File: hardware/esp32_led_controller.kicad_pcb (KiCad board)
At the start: 4 copper layers, 61 x 42.5 mm, 28 parts, among them J1 USB_B, J2 BARREL_JACK, J3 Screw_Terminal_1x03, J4 CONN_01X11, J5 CONN_01X09, Q1 Q_NPN_BEC, Q4 Q_NPN_BEC, SW1 SW_Push, U1 MCP1415, U11 AZ1117-3.3, U3 CP2102, U4 ESP32-WROOM-32

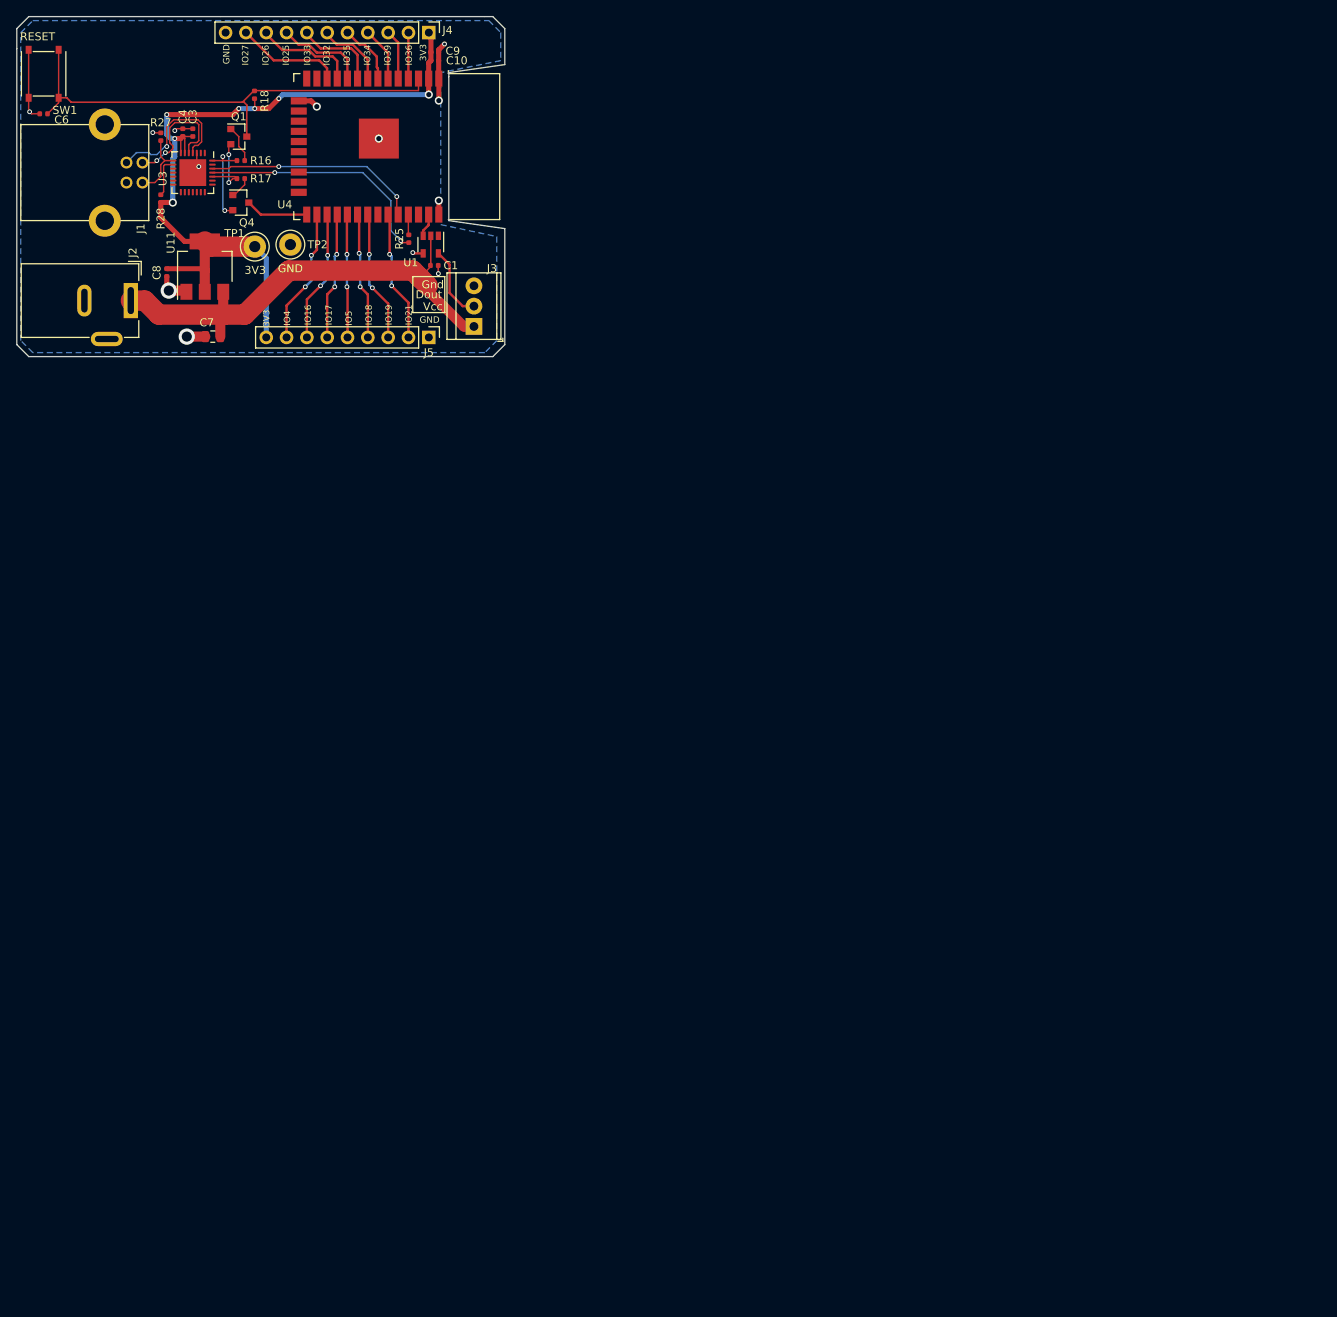
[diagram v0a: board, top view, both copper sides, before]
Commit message: Finished design with integrated LED matrix
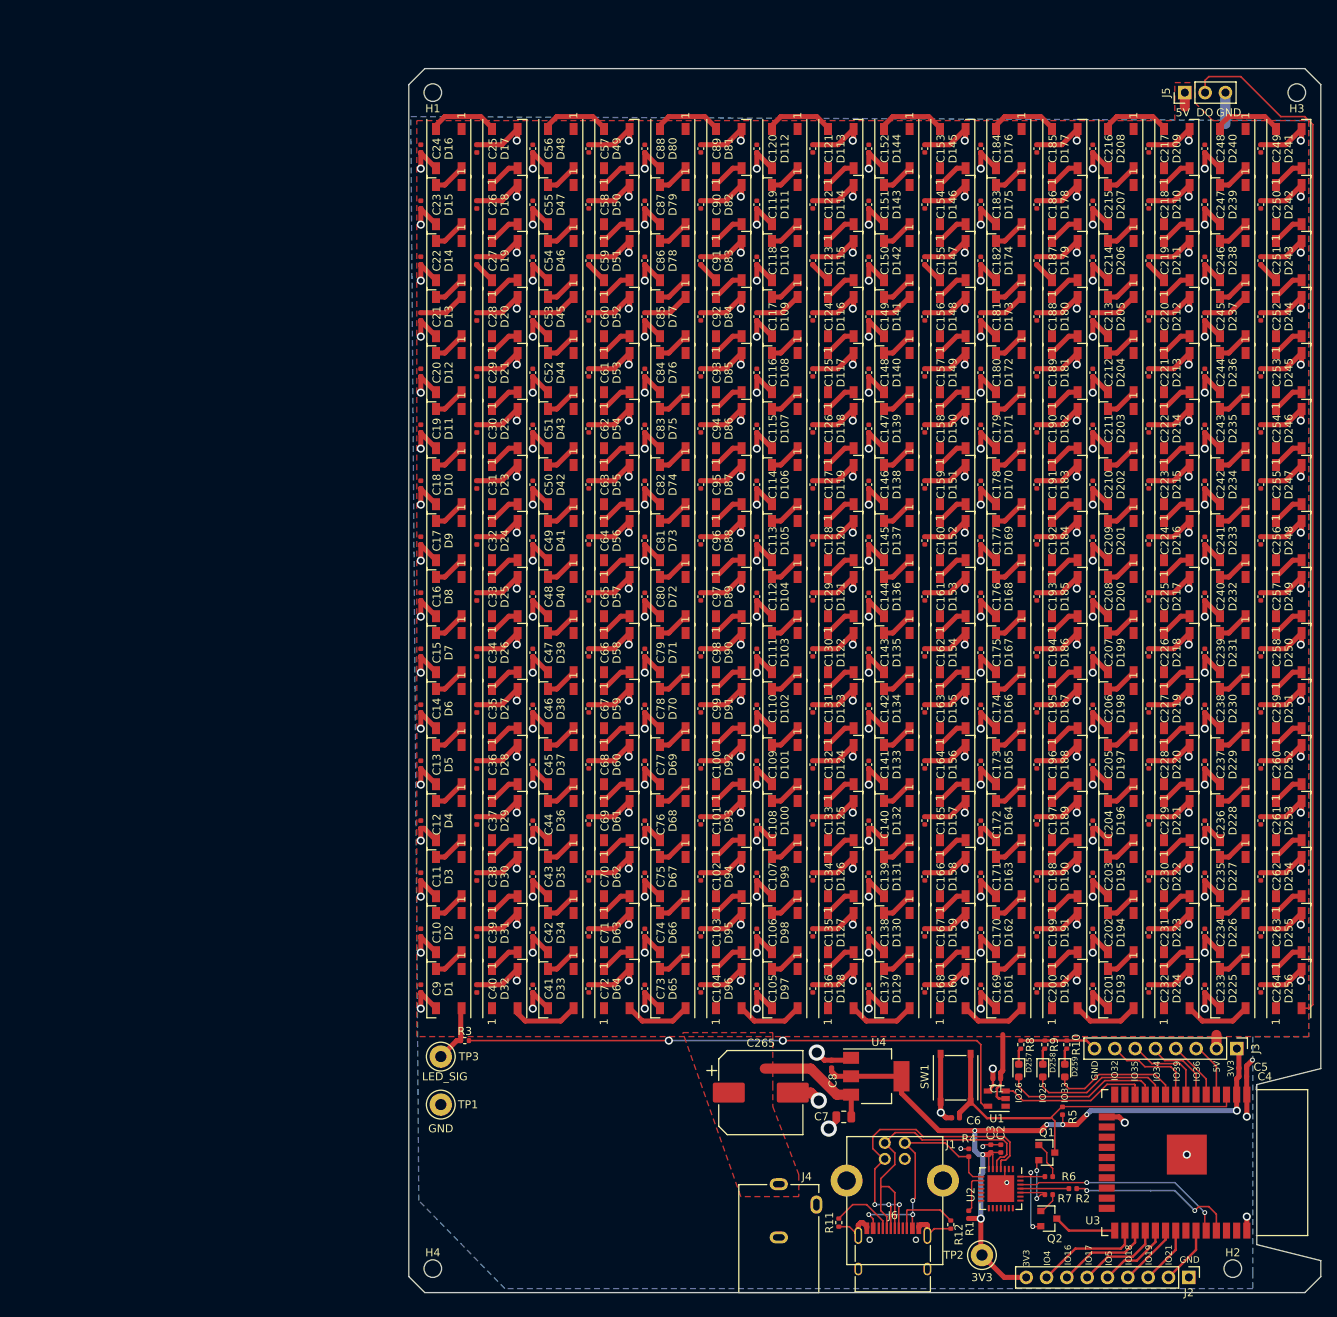
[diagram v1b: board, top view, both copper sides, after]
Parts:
- removed the J2 at (93.2, 75.0)
- added C10: 0.1uF, Capacitor_SMD:C_0402_1005Metric, F.Cu at (129.5, 154.0)
- added C100: 0.1uF, Capacitor_SMD:C_0402_1005Metric, F.Cu at (164.5, 133.0)
- added C101: 0.1uF, Capacitor_SMD:C_0402_1005Metric, F.Cu at (164.5, 140.0)
- added C102: 0.1uF, Capacitor_SMD:C_0402_1005Metric, F.Cu at (164.5, 147.0)
- added C103: 0.1uF, Capacitor_SMD:C_0402_1005Metric, F.Cu at (164.5, 154.0)
- added C104: 0.1uF, Capacitor_SMD:C_0402_1005Metric, F.Cu at (164.5, 161.0)
- added C105: 0.1uF, Capacitor_SMD:C_0402_1005Metric, F.Cu at (171.5, 161.0)
- added C106: 0.1uF, Capacitor_SMD:C_0402_1005Metric, F.Cu at (171.5, 154.0)
- added C107: 0.1uF, Capacitor_SMD:C_0402_1005Metric, F.Cu at (171.5, 147.0)
- added C108: 0.1uF, Capacitor_SMD:C_0402_1005Metric, F.Cu at (171.5, 140.5)
- added C109: 0.1uF, Capacitor_SMD:C_0402_1005Metric, F.Cu at (171.5, 133.0)
- added C11: 0.1uF, Capacitor_SMD:C_0402_1005Metric, F.Cu at (129.5, 147.0)
- added C110: 0.1uF, Capacitor_SMD:C_0402_1005Metric, F.Cu at (171.5, 126.0)
- added C111: 0.1uF, Capacitor_SMD:C_0402_1005Metric, F.Cu at (171.5, 119.0)
- added C112: 0.1uF, Capacitor_SMD:C_0402_1005Metric, F.Cu at (171.5, 112.0)
- added C113: 0.1uF, Capacitor_SMD:C_0402_1005Metric, F.Cu at (171.5, 105.0)
- added C114: 0.1uF, Capacitor_SMD:C_0402_1005Metric, F.Cu at (171.5, 98.0)
- added C115: 0.1uF, Capacitor_SMD:C_0402_1005Metric, F.Cu at (171.5, 91.0)
- added C116: 0.1uF, Capacitor_SMD:C_0402_1005Metric, F.Cu at (171.5, 84.0)
- added C117: 0.1uF, Capacitor_SMD:C_0402_1005Metric, F.Cu at (171.5, 77.0)
- added C118: 0.1uF, Capacitor_SMD:C_0402_1005Metric, F.Cu at (171.5, 70.0)
- added C119: 0.1uF, Capacitor_SMD:C_0402_1005Metric, F.Cu at (171.5, 63.0)
- added C12: 0.1uF, Capacitor_SMD:C_0402_1005Metric, F.Cu at (129.5, 140.5)
- added C120: 0.1uF, Capacitor_SMD:C_0402_1005Metric, F.Cu at (171.5, 56.0)
- added C121: 0.1uF, Capacitor_SMD:C_0402_1005Metric, F.Cu at (178.5, 56.0)
- added C122: 0.1uF, Capacitor_SMD:C_0402_1005Metric, F.Cu at (178.5, 63.0)
- added C123: 0.1uF, Capacitor_SMD:C_0402_1005Metric, F.Cu at (178.5, 70.0)
- added C124: 0.1uF, Capacitor_SMD:C_0402_1005Metric, F.Cu at (178.5, 77.0)
- added C125: 0.1uF, Capacitor_SMD:C_0402_1005Metric, F.Cu at (178.5, 84.0)
- added C126: 0.1uF, Capacitor_SMD:C_0402_1005Metric, F.Cu at (178.5, 91.0)
- added C127: 0.1uF, Capacitor_SMD:C_0402_1005Metric, F.Cu at (178.5, 98.0)
- added C128: 0.1uF, Capacitor_SMD:C_0402_1005Metric, F.Cu at (178.5, 105.0)
- added C129: 0.1uF, Capacitor_SMD:C_0402_1005Metric, F.Cu at (178.5, 112.0)
- added C13: 0.1uF, Capacitor_SMD:C_0402_1005Metric, F.Cu at (129.5, 133.0)
- added C130: 0.1uF, Capacitor_SMD:C_0402_1005Metric, F.Cu at (178.5, 119.0)
- added C131: 0.1uF, Capacitor_SMD:C_0402_1005Metric, F.Cu at (178.5, 126.0)
- added C132: 0.1uF, Capacitor_SMD:C_0402_1005Metric, F.Cu at (178.5, 133.0)
- added C133: 0.1uF, Capacitor_SMD:C_0402_1005Metric, F.Cu at (178.5, 140.0)
- added C134: 0.1uF, Capacitor_SMD:C_0402_1005Metric, F.Cu at (178.5, 147.0)
- added C135: 0.1uF, Capacitor_SMD:C_0402_1005Metric, F.Cu at (178.5, 154.0)
- added C136: 0.1uF, Capacitor_SMD:C_0402_1005Metric, F.Cu at (178.5, 161.0)
- added C137: 0.1uF, Capacitor_SMD:C_0402_1005Metric, F.Cu at (185.5, 161.0)
- added C138: 0.1uF, Capacitor_SMD:C_0402_1005Metric, F.Cu at (185.5, 154.0)
- added C139: 0.1uF, Capacitor_SMD:C_0402_1005Metric, F.Cu at (185.5, 147.0)
- added C14: 0.1uF, Capacitor_SMD:C_0402_1005Metric, F.Cu at (129.5, 126.0)
- added C140: 0.1uF, Capacitor_SMD:C_0402_1005Metric, F.Cu at (185.5, 140.5)
- added C141: 0.1uF, Capacitor_SMD:C_0402_1005Metric, F.Cu at (185.5, 133.0)
- added C142: 0.1uF, Capacitor_SMD:C_0402_1005Metric, F.Cu at (185.5, 126.0)
- added C143: 0.1uF, Capacitor_SMD:C_0402_1005Metric, F.Cu at (185.5, 119.0)
- added C144: 0.1uF, Capacitor_SMD:C_0402_1005Metric, F.Cu at (185.5, 112.0)
- added C145: 0.1uF, Capacitor_SMD:C_0402_1005Metric, F.Cu at (185.5, 105.0)
- added C146: 0.1uF, Capacitor_SMD:C_0402_1005Metric, F.Cu at (185.5, 98.0)
- added C147: 0.1uF, Capacitor_SMD:C_0402_1005Metric, F.Cu at (185.5, 91.0)
- added C148: 0.1uF, Capacitor_SMD:C_0402_1005Metric, F.Cu at (185.5, 84.0)
- added C149: 0.1uF, Capacitor_SMD:C_0402_1005Metric, F.Cu at (185.5, 77.0)
- added C15: 0.1uF, Capacitor_SMD:C_0402_1005Metric, F.Cu at (129.5, 119.0)
- added C150: 0.1uF, Capacitor_SMD:C_0402_1005Metric, F.Cu at (185.5, 70.0)
- added C151: 0.1uF, Capacitor_SMD:C_0402_1005Metric, F.Cu at (185.5, 63.0)
- added C152: 0.1uF, Capacitor_SMD:C_0402_1005Metric, F.Cu at (185.5, 56.0)
- added C153: 0.1uF, Capacitor_SMD:C_0402_1005Metric, F.Cu at (192.5, 56.0)
- added C154: 0.1uF, Capacitor_SMD:C_0402_1005Metric, F.Cu at (192.5, 63.0)
- added C155: 0.1uF, Capacitor_SMD:C_0402_1005Metric, F.Cu at (192.5, 70.0)
- added C156: 0.1uF, Capacitor_SMD:C_0402_1005Metric, F.Cu at (192.5, 77.0)
- added C157: 0.1uF, Capacitor_SMD:C_0402_1005Metric, F.Cu at (192.5, 84.0)
- added C158: 0.1uF, Capacitor_SMD:C_0402_1005Metric, F.Cu at (192.5, 91.0)
- added C159: 0.1uF, Capacitor_SMD:C_0402_1005Metric, F.Cu at (192.5, 98.0)
- added C16: 0.1uF, Capacitor_SMD:C_0402_1005Metric, F.Cu at (129.5, 112.0)
- added C160: 0.1uF, Capacitor_SMD:C_0402_1005Metric, F.Cu at (192.5, 105.0)
- added C161: 0.1uF, Capacitor_SMD:C_0402_1005Metric, F.Cu at (192.5, 112.0)
- added C162: 0.1uF, Capacitor_SMD:C_0402_1005Metric, F.Cu at (192.5, 119.0)
- added C163: 0.1uF, Capacitor_SMD:C_0402_1005Metric, F.Cu at (192.5, 126.0)
- added C164: 0.1uF, Capacitor_SMD:C_0402_1005Metric, F.Cu at (192.5, 133.0)
- added C165: 0.1uF, Capacitor_SMD:C_0402_1005Metric, F.Cu at (192.5, 140.0)
- added C166: 0.1uF, Capacitor_SMD:C_0402_1005Metric, F.Cu at (192.5, 147.0)
- added C167: 0.1uF, Capacitor_SMD:C_0402_1005Metric, F.Cu at (192.5, 154.0)
- added C168: 0.1uF, Capacitor_SMD:C_0402_1005Metric, F.Cu at (192.5, 161.0)
- added C169: 0.1uF, Capacitor_SMD:C_0402_1005Metric, F.Cu at (199.5, 161.0)
- added C17: 0.1uF, Capacitor_SMD:C_0402_1005Metric, F.Cu at (129.5, 105.0)
- added C170: 0.1uF, Capacitor_SMD:C_0402_1005Metric, F.Cu at (199.5, 154.0)
- added C171: 0.1uF, Capacitor_SMD:C_0402_1005Metric, F.Cu at (199.5, 147.0)
- added C172: 0.1uF, Capacitor_SMD:C_0402_1005Metric, F.Cu at (199.5, 140.5)
- added C173: 0.1uF, Capacitor_SMD:C_0402_1005Metric, F.Cu at (199.5, 133.0)
- added C174: 0.1uF, Capacitor_SMD:C_0402_1005Metric, F.Cu at (199.5, 126.0)
- added C175: 0.1uF, Capacitor_SMD:C_0402_1005Metric, F.Cu at (199.5, 119.0)
- added C176: 0.1uF, Capacitor_SMD:C_0402_1005Metric, F.Cu at (199.5, 112.0)
- added C177: 0.1uF, Capacitor_SMD:C_0402_1005Metric, F.Cu at (199.5, 105.0)
- added C178: 0.1uF, Capacitor_SMD:C_0402_1005Metric, F.Cu at (199.5, 98.0)
- added C179: 0.1uF, Capacitor_SMD:C_0402_1005Metric, F.Cu at (199.5, 91.0)
- added C18: 0.1uF, Capacitor_SMD:C_0402_1005Metric, F.Cu at (129.5, 98.0)
- added C180: 0.1uF, Capacitor_SMD:C_0402_1005Metric, F.Cu at (199.5, 84.0)
- added C181: 0.1uF, Capacitor_SMD:C_0402_1005Metric, F.Cu at (199.5, 77.0)
- added C182: 0.1uF, Capacitor_SMD:C_0402_1005Metric, F.Cu at (199.5, 70.0)
- added C183: 0.1uF, Capacitor_SMD:C_0402_1005Metric, F.Cu at (199.5, 63.0)
- added C184: 0.1uF, Capacitor_SMD:C_0402_1005Metric, F.Cu at (199.5, 56.0)
- added C185: 0.1uF, Capacitor_SMD:C_0402_1005Metric, F.Cu at (206.5, 56.0)
- added C186: 0.1uF, Capacitor_SMD:C_0402_1005Metric, F.Cu at (206.5, 63.0)
- added C187: 0.1uF, Capacitor_SMD:C_0402_1005Metric, F.Cu at (206.5, 70.0)
- added C188: 0.1uF, Capacitor_SMD:C_0402_1005Metric, F.Cu at (206.5, 77.0)
- added C189: 0.1uF, Capacitor_SMD:C_0402_1005Metric, F.Cu at (206.5, 84.0)
- added C19: 0.1uF, Capacitor_SMD:C_0402_1005Metric, F.Cu at (129.5, 91.0)
- added C190: 0.1uF, Capacitor_SMD:C_0402_1005Metric, F.Cu at (206.5, 91.0)
- added C191: 0.1uF, Capacitor_SMD:C_0402_1005Metric, F.Cu at (206.5, 98.0)
- added C192: 0.1uF, Capacitor_SMD:C_0402_1005Metric, F.Cu at (206.5, 105.0)
- added C193: 0.1uF, Capacitor_SMD:C_0402_1005Metric, F.Cu at (206.5, 112.0)
- added C194: 0.1uF, Capacitor_SMD:C_0402_1005Metric, F.Cu at (206.5, 119.0)
- added C195: 0.1uF, Capacitor_SMD:C_0402_1005Metric, F.Cu at (206.5, 126.0)
- added C196: 0.1uF, Capacitor_SMD:C_0402_1005Metric, F.Cu at (206.5, 133.0)
- added C197: 0.1uF, Capacitor_SMD:C_0402_1005Metric, F.Cu at (206.5, 140.0)
- added C198: 0.1uF, Capacitor_SMD:C_0402_1005Metric, F.Cu at (206.5, 147.0)
- added C199: 0.1uF, Capacitor_SMD:C_0402_1005Metric, F.Cu at (206.5, 154.0)
- added C20: 0.1uF, Capacitor_SMD:C_0402_1005Metric, F.Cu at (129.5, 84.0)
- added C200: 0.1uF, Capacitor_SMD:C_0402_1005Metric, F.Cu at (206.5, 161.0)
- added C201: 0.1uF, Capacitor_SMD:C_0402_1005Metric, F.Cu at (213.5, 161.0)
- added C202: 0.1uF, Capacitor_SMD:C_0402_1005Metric, F.Cu at (213.5, 154.0)
- added C203: 0.1uF, Capacitor_SMD:C_0402_1005Metric, F.Cu at (213.5, 147.0)
- added C204: 0.1uF, Capacitor_SMD:C_0402_1005Metric, F.Cu at (213.5, 140.5)
- added C205: 0.1uF, Capacitor_SMD:C_0402_1005Metric, F.Cu at (213.5, 133.0)
- added C206: 0.1uF, Capacitor_SMD:C_0402_1005Metric, F.Cu at (213.5, 126.0)
- added C207: 0.1uF, Capacitor_SMD:C_0402_1005Metric, F.Cu at (213.5, 119.0)
- added C208: 0.1uF, Capacitor_SMD:C_0402_1005Metric, F.Cu at (213.5, 112.0)
- added C209: 0.1uF, Capacitor_SMD:C_0402_1005Metric, F.Cu at (213.5, 105.0)
- added C21: 0.1uF, Capacitor_SMD:C_0402_1005Metric, F.Cu at (129.5, 77.0)
- added C210: 0.1uF, Capacitor_SMD:C_0402_1005Metric, F.Cu at (213.5, 98.0)
- added C211: 0.1uF, Capacitor_SMD:C_0402_1005Metric, F.Cu at (213.5, 91.0)
- added C212: 0.1uF, Capacitor_SMD:C_0402_1005Metric, F.Cu at (213.5, 84.0)
- added C213: 0.1uF, Capacitor_SMD:C_0402_1005Metric, F.Cu at (213.5, 77.0)
- added C214: 0.1uF, Capacitor_SMD:C_0402_1005Metric, F.Cu at (213.5, 70.0)
- added C215: 0.1uF, Capacitor_SMD:C_0402_1005Metric, F.Cu at (213.5, 63.0)
- added C216: 0.1uF, Capacitor_SMD:C_0402_1005Metric, F.Cu at (213.5, 56.0)
- added C217: 0.1uF, Capacitor_SMD:C_0402_1005Metric, F.Cu at (220.5, 56.0)
- added C218: 0.1uF, Capacitor_SMD:C_0402_1005Metric, F.Cu at (220.5, 63.0)
- added C219: 0.1uF, Capacitor_SMD:C_0402_1005Metric, F.Cu at (220.5, 70.0)
- added C22: 0.1uF, Capacitor_SMD:C_0402_1005Metric, F.Cu at (129.5, 70.0)
- added C220: 0.1uF, Capacitor_SMD:C_0402_1005Metric, F.Cu at (220.5, 77.0)
- added C221: 0.1uF, Capacitor_SMD:C_0402_1005Metric, F.Cu at (220.5, 84.0)
- added C222: 0.1uF, Capacitor_SMD:C_0402_1005Metric, F.Cu at (220.5, 91.0)
- added C223: 0.1uF, Capacitor_SMD:C_0402_1005Metric, F.Cu at (220.5, 98.0)
- added C224: 0.1uF, Capacitor_SMD:C_0402_1005Metric, F.Cu at (220.5, 105.0)
- added C225: 0.1uF, Capacitor_SMD:C_0402_1005Metric, F.Cu at (220.5, 112.0)
- added C226: 0.1uF, Capacitor_SMD:C_0402_1005Metric, F.Cu at (220.5, 119.0)
- added C227: 0.1uF, Capacitor_SMD:C_0402_1005Metric, F.Cu at (220.5, 126.0)
- added C228: 0.1uF, Capacitor_SMD:C_0402_1005Metric, F.Cu at (220.5, 133.0)
- added C229: 0.1uF, Capacitor_SMD:C_0402_1005Metric, F.Cu at (220.5, 140.0)
- added C23: 0.1uF, Capacitor_SMD:C_0402_1005Metric, F.Cu at (129.5, 63.0)
- added C230: 0.1uF, Capacitor_SMD:C_0402_1005Metric, F.Cu at (220.5, 147.0)
- added C231: 0.1uF, Capacitor_SMD:C_0402_1005Metric, F.Cu at (220.5, 154.0)
- added C232: 0.1uF, Capacitor_SMD:C_0402_1005Metric, F.Cu at (220.5, 161.0)
- added C233: 0.1uF, Capacitor_SMD:C_0402_1005Metric, F.Cu at (227.5, 161.0)
- added C234: 0.1uF, Capacitor_SMD:C_0402_1005Metric, F.Cu at (227.5, 154.0)
- added C235: 0.1uF, Capacitor_SMD:C_0402_1005Metric, F.Cu at (227.5, 147.0)
- added C236: 0.1uF, Capacitor_SMD:C_0402_1005Metric, F.Cu at (227.5, 140.5)
- added C237: 0.1uF, Capacitor_SMD:C_0402_1005Metric, F.Cu at (227.5, 133.0)
- added C238: 0.1uF, Capacitor_SMD:C_0402_1005Metric, F.Cu at (227.5, 126.0)
- added C239: 0.1uF, Capacitor_SMD:C_0402_1005Metric, F.Cu at (227.5, 119.0)
- added C24: 0.1uF, Capacitor_SMD:C_0402_1005Metric, F.Cu at (129.5, 56.0)
- added C240: 0.1uF, Capacitor_SMD:C_0402_1005Metric, F.Cu at (227.5, 112.0)
- added C241: 0.1uF, Capacitor_SMD:C_0402_1005Metric, F.Cu at (227.5, 105.0)
- added C242: 0.1uF, Capacitor_SMD:C_0402_1005Metric, F.Cu at (227.5, 98.0)
- added C243: 0.1uF, Capacitor_SMD:C_0402_1005Metric, F.Cu at (227.5, 91.0)
- added C244: 0.1uF, Capacitor_SMD:C_0402_1005Metric, F.Cu at (227.5, 84.0)
- added C245: 0.1uF, Capacitor_SMD:C_0402_1005Metric, F.Cu at (227.5, 77.0)
- added C246: 0.1uF, Capacitor_SMD:C_0402_1005Metric, F.Cu at (227.5, 70.0)
- added C247: 0.1uF, Capacitor_SMD:C_0402_1005Metric, F.Cu at (227.5, 63.0)
- added C248: 0.1uF, Capacitor_SMD:C_0402_1005Metric, F.Cu at (227.5, 56.0)
- added C249: 0.1uF, Capacitor_SMD:C_0402_1005Metric, F.Cu at (234.5, 56.0)
- added C25: 0.1uF, Capacitor_SMD:C_0402_1005Metric, F.Cu at (136.5, 56.0)
- added C250: 0.1uF, Capacitor_SMD:C_0402_1005Metric, F.Cu at (234.5, 63.0)
- added C251: 0.1uF, Capacitor_SMD:C_0402_1005Metric, F.Cu at (234.5, 70.0)
- added C252: 0.1uF, Capacitor_SMD:C_0402_1005Metric, F.Cu at (234.5, 77.0)
- added C253: 0.1uF, Capacitor_SMD:C_0402_1005Metric, F.Cu at (234.5, 84.0)
- added C254: 0.1uF, Capacitor_SMD:C_0402_1005Metric, F.Cu at (234.5, 91.0)
- added C255: 0.1uF, Capacitor_SMD:C_0402_1005Metric, F.Cu at (234.5, 98.0)
- added C256: 0.1uF, Capacitor_SMD:C_0402_1005Metric, F.Cu at (234.5, 105.0)
- added C257: 0.1uF, Capacitor_SMD:C_0402_1005Metric, F.Cu at (234.5, 112.0)
- added C258: 0.1uF, Capacitor_SMD:C_0402_1005Metric, F.Cu at (234.5, 119.0)
- added C259: 0.1uF, Capacitor_SMD:C_0402_1005Metric, F.Cu at (234.5, 126.0)
- added C26: 0.1uF, Capacitor_SMD:C_0402_1005Metric, F.Cu at (136.5, 63.0)
- added C260: 0.1uF, Capacitor_SMD:C_0402_1005Metric, F.Cu at (234.5, 133.0)
- added C261: 0.1uF, Capacitor_SMD:C_0402_1005Metric, F.Cu at (234.5, 140.0)
- added C262: 0.1uF, Capacitor_SMD:C_0402_1005Metric, F.Cu at (234.5, 147.0)
- added C263: 0.1uF, Capacitor_SMD:C_0402_1005Metric, F.Cu at (234.5, 154.0)
- added C264: 0.1uF, Capacitor_SMD:C_0402_1005Metric, F.Cu at (234.5, 161.0)
- added C265: 1000uF, Capacitor_SMD:CP_Elec_10x10, F.Cu at (172.0, 174.0)
- added C27: 0.1uF, Capacitor_SMD:C_0402_1005Metric, F.Cu at (136.5, 70.0)
- added C28: 0.1uF, Capacitor_SMD:C_0402_1005Metric, F.Cu at (136.5, 77.0)
- added C29: 0.1uF, Capacitor_SMD:C_0402_1005Metric, F.Cu at (136.5, 84.0)
- added C30: 0.1uF, Capacitor_SMD:C_0402_1005Metric, F.Cu at (136.5, 91.0)
- added C31: 0.1uF, Capacitor_SMD:C_0402_1005Metric, F.Cu at (136.5, 98.0)
- added C32: 0.1uF, Capacitor_SMD:C_0402_1005Metric, F.Cu at (136.5, 105.0)
- added C33: 0.1uF, Capacitor_SMD:C_0402_1005Metric, F.Cu at (136.5, 112.0)
- added C34: 0.1uF, Capacitor_SMD:C_0402_1005Metric, F.Cu at (136.5, 119.0)
- added C35: 0.1uF, Capacitor_SMD:C_0402_1005Metric, F.Cu at (136.5, 126.0)
- added C36: 0.1uF, Capacitor_SMD:C_0402_1005Metric, F.Cu at (136.5, 133.0)
- added C37: 0.1uF, Capacitor_SMD:C_0402_1005Metric, F.Cu at (136.5, 140.0)
- added C38: 0.1uF, Capacitor_SMD:C_0402_1005Metric, F.Cu at (136.5, 147.0)
- added C39: 0.1uF, Capacitor_SMD:C_0402_1005Metric, F.Cu at (136.5, 154.0)
- added C40: 0.1uF, Capacitor_SMD:C_0402_1005Metric, F.Cu at (136.5, 161.0)
- added C41: 0.1uF, Capacitor_SMD:C_0402_1005Metric, F.Cu at (143.5, 161.0)
- added C42: 0.1uF, Capacitor_SMD:C_0402_1005Metric, F.Cu at (143.5, 154.0)
- added C43: 0.1uF, Capacitor_SMD:C_0402_1005Metric, F.Cu at (143.5, 147.0)
- added C44: 0.1uF, Capacitor_SMD:C_0402_1005Metric, F.Cu at (143.5, 140.5)
- added C45: 0.1uF, Capacitor_SMD:C_0402_1005Metric, F.Cu at (143.5, 133.0)
- added C46: 0.1uF, Capacitor_SMD:C_0402_1005Metric, F.Cu at (143.5, 126.0)
- added C47: 0.1uF, Capacitor_SMD:C_0402_1005Metric, F.Cu at (143.5, 119.0)
- added C48: 0.1uF, Capacitor_SMD:C_0402_1005Metric, F.Cu at (143.5, 112.0)
- added C49: 0.1uF, Capacitor_SMD:C_0402_1005Metric, F.Cu at (143.5, 105.0)
- added C50: 0.1uF, Capacitor_SMD:C_0402_1005Metric, F.Cu at (143.5, 98.0)
- added C51: 0.1uF, Capacitor_SMD:C_0402_1005Metric, F.Cu at (143.5, 91.0)
- added C52: 0.1uF, Capacitor_SMD:C_0402_1005Metric, F.Cu at (143.5, 84.0)
- added C53: 0.1uF, Capacitor_SMD:C_0402_1005Metric, F.Cu at (143.5, 77.0)
- added C54: 0.1uF, Capacitor_SMD:C_0402_1005Metric, F.Cu at (143.5, 70.0)
- added C55: 0.1uF, Capacitor_SMD:C_0402_1005Metric, F.Cu at (143.5, 63.0)
- added C56: 0.1uF, Capacitor_SMD:C_0402_1005Metric, F.Cu at (143.5, 56.0)
- added C57: 0.1uF, Capacitor_SMD:C_0402_1005Metric, F.Cu at (150.5, 56.0)
- added C58: 0.1uF, Capacitor_SMD:C_0402_1005Metric, F.Cu at (150.5, 63.0)
- added C59: 0.1uF, Capacitor_SMD:C_0402_1005Metric, F.Cu at (150.5, 70.0)
- added C60: 0.1uF, Capacitor_SMD:C_0402_1005Metric, F.Cu at (150.5, 77.0)
- added C61: 0.1uF, Capacitor_SMD:C_0402_1005Metric, F.Cu at (150.5, 84.0)
- added C62: 0.1uF, Capacitor_SMD:C_0402_1005Metric, F.Cu at (150.5, 91.0)
- added C63: 0.1uF, Capacitor_SMD:C_0402_1005Metric, F.Cu at (150.5, 98.0)
- added C64: 0.1uF, Capacitor_SMD:C_0402_1005Metric, F.Cu at (150.5, 105.0)
- added C65: 0.1uF, Capacitor_SMD:C_0402_1005Metric, F.Cu at (150.5, 112.0)
- added C66: 0.1uF, Capacitor_SMD:C_0402_1005Metric, F.Cu at (150.5, 119.0)
- added C67: 0.1uF, Capacitor_SMD:C_0402_1005Metric, F.Cu at (150.5, 126.0)
- added C68: 0.1uF, Capacitor_SMD:C_0402_1005Metric, F.Cu at (150.5, 133.0)
- added C69: 0.1uF, Capacitor_SMD:C_0402_1005Metric, F.Cu at (150.5, 140.0)
- added C70: 0.1uF, Capacitor_SMD:C_0402_1005Metric, F.Cu at (150.5, 147.0)
- added C71: 0.1uF, Capacitor_SMD:C_0402_1005Metric, F.Cu at (150.5, 154.0)
- added C72: 0.1uF, Capacitor_SMD:C_0402_1005Metric, F.Cu at (150.5, 161.0)
- added C73: 0.1uF, Capacitor_SMD:C_0402_1005Metric, F.Cu at (157.5, 161.0)
- added C74: 0.1uF, Capacitor_SMD:C_0402_1005Metric, F.Cu at (157.5, 154.0)
- added C75: 0.1uF, Capacitor_SMD:C_0402_1005Metric, F.Cu at (157.5, 147.0)
- added C76: 0.1uF, Capacitor_SMD:C_0402_1005Metric, F.Cu at (157.5, 140.5)
- added C77: 0.1uF, Capacitor_SMD:C_0402_1005Metric, F.Cu at (157.5, 133.0)
- added C78: 0.1uF, Capacitor_SMD:C_0402_1005Metric, F.Cu at (157.5, 126.0)
- added C79: 0.1uF, Capacitor_SMD:C_0402_1005Metric, F.Cu at (157.5, 119.0)
- added C80: 0.1uF, Capacitor_SMD:C_0402_1005Metric, F.Cu at (157.5, 112.0)
- added C81: 0.1uF, Capacitor_SMD:C_0402_1005Metric, F.Cu at (157.5, 105.0)
- added C82: 0.1uF, Capacitor_SMD:C_0402_1005Metric, F.Cu at (157.5, 98.0)
- added C83: 0.1uF, Capacitor_SMD:C_0402_1005Metric, F.Cu at (157.5, 91.0)
- added C84: 0.1uF, Capacitor_SMD:C_0402_1005Metric, F.Cu at (157.5, 84.0)
- added C85: 0.1uF, Capacitor_SMD:C_0402_1005Metric, F.Cu at (157.5, 77.0)
- added C86: 0.1uF, Capacitor_SMD:C_0402_1005Metric, F.Cu at (157.5, 70.0)
- added C87: 0.1uF, Capacitor_SMD:C_0402_1005Metric, F.Cu at (157.5, 63.0)
- added C88: 0.1uF, Capacitor_SMD:C_0402_1005Metric, F.Cu at (157.5, 56.0)
- added C89: 0.1uF, Capacitor_SMD:C_0402_1005Metric, F.Cu at (164.5, 56.0)
- added C9: 0.1uF, Capacitor_SMD:C_0402_1005Metric, F.Cu at (129.5, 161.0)
- added C90: 0.1uF, Capacitor_SMD:C_0402_1005Metric, F.Cu at (164.5, 63.0)
- added C91: 0.1uF, Capacitor_SMD:C_0402_1005Metric, F.Cu at (164.5, 70.0)
- added C92: 0.1uF, Capacitor_SMD:C_0402_1005Metric, F.Cu at (164.5, 77.0)
- added C93: 0.1uF, Capacitor_SMD:C_0402_1005Metric, F.Cu at (164.5, 84.0)
- added C94: 0.1uF, Capacitor_SMD:C_0402_1005Metric, F.Cu at (164.5, 91.0)
- added C95: 0.1uF, Capacitor_SMD:C_0402_1005Metric, F.Cu at (164.5, 98.0)
- added C96: 0.1uF, Capacitor_SMD:C_0402_1005Metric, F.Cu at (164.5, 105.0)
- added C97: 0.1uF, Capacitor_SMD:C_0402_1005Metric, F.Cu at (164.5, 112.0)
- added C98: 0.1uF, Capacitor_SMD:C_0402_1005Metric, F.Cu at (164.5, 119.0)
- added C99: 0.1uF, Capacitor_SMD:C_0402_1005Metric, F.Cu at (164.5, 126.0)
- added D1: WS2812B, LED_SMD:LED_WS2812B_PLCC4_5.0x5.0mm_P3.2mm, F.Cu at (133.0, 161.0)
- added D10: WS2812B, LED_SMD:LED_WS2812B_PLCC4_5.0x5.0mm_P3.2mm, F.Cu at (133.0, 98.0)
- added D100: WS2812B, LED_SMD:LED_WS2812B_PLCC4_5.0x5.0mm_P3.2mm, F.Cu at (175.0, 140.0)
- added D101: WS2812B, LED_SMD:LED_WS2812B_PLCC4_5.0x5.0mm_P3.2mm, F.Cu at (175.0, 133.0)
- added D102: WS2812B, LED_SMD:LED_WS2812B_PLCC4_5.0x5.0mm_P3.2mm, F.Cu at (175.0, 126.0)
- added D103: WS2812B, LED_SMD:LED_WS2812B_PLCC4_5.0x5.0mm_P3.2mm, F.Cu at (175.0, 119.0)
- added D104: WS2812B, LED_SMD:LED_WS2812B_PLCC4_5.0x5.0mm_P3.2mm, F.Cu at (175.0, 112.0)
- added D105: WS2812B, LED_SMD:LED_WS2812B_PLCC4_5.0x5.0mm_P3.2mm, F.Cu at (175.0, 105.0)
- added D106: WS2812B, LED_SMD:LED_WS2812B_PLCC4_5.0x5.0mm_P3.2mm, F.Cu at (175.0, 98.0)
- added D107: WS2812B, LED_SMD:LED_WS2812B_PLCC4_5.0x5.0mm_P3.2mm, F.Cu at (175.0, 91.0)
- added D108: WS2812B, LED_SMD:LED_WS2812B_PLCC4_5.0x5.0mm_P3.2mm, F.Cu at (175.0, 84.0)
- added D109: WS2812B, LED_SMD:LED_WS2812B_PLCC4_5.0x5.0mm_P3.2mm, F.Cu at (175.0, 77.0)
- added D11: WS2812B, LED_SMD:LED_WS2812B_PLCC4_5.0x5.0mm_P3.2mm, F.Cu at (133.0, 91.0)
- added D110: WS2812B, LED_SMD:LED_WS2812B_PLCC4_5.0x5.0mm_P3.2mm, F.Cu at (175.0, 70.0)
- added D111: WS2812B, LED_SMD:LED_WS2812B_PLCC4_5.0x5.0mm_P3.2mm, F.Cu at (175.0, 63.0)
- added D112: WS2812B, LED_SMD:LED_WS2812B_PLCC4_5.0x5.0mm_P3.2mm, F.Cu at (175.0, 56.0)
- added D113: WS2812B, LED_SMD:LED_WS2812B_PLCC4_5.0x5.0mm_P3.2mm, F.Cu at (182.0, 56.0)
- added D114: WS2812B, LED_SMD:LED_WS2812B_PLCC4_5.0x5.0mm_P3.2mm, F.Cu at (182.0, 63.0)
- added D115: WS2812B, LED_SMD:LED_WS2812B_PLCC4_5.0x5.0mm_P3.2mm, F.Cu at (182.0, 70.0)
- added D116: WS2812B, LED_SMD:LED_WS2812B_PLCC4_5.0x5.0mm_P3.2mm, F.Cu at (182.0, 77.0)
- added D117: WS2812B, LED_SMD:LED_WS2812B_PLCC4_5.0x5.0mm_P3.2mm, F.Cu at (182.0, 84.0)
- added D118: WS2812B, LED_SMD:LED_WS2812B_PLCC4_5.0x5.0mm_P3.2mm, F.Cu at (182.0, 91.0)
- added D119: WS2812B, LED_SMD:LED_WS2812B_PLCC4_5.0x5.0mm_P3.2mm, F.Cu at (182.0, 98.0)
- added D12: WS2812B, LED_SMD:LED_WS2812B_PLCC4_5.0x5.0mm_P3.2mm, F.Cu at (133.0, 84.0)
- added D120: WS2812B, LED_SMD:LED_WS2812B_PLCC4_5.0x5.0mm_P3.2mm, F.Cu at (182.0, 105.0)
- added D121: WS2812B, LED_SMD:LED_WS2812B_PLCC4_5.0x5.0mm_P3.2mm, F.Cu at (182.0, 112.0)
- added D122: WS2812B, LED_SMD:LED_WS2812B_PLCC4_5.0x5.0mm_P3.2mm, F.Cu at (182.0, 119.0)
- added D123: WS2812B, LED_SMD:LED_WS2812B_PLCC4_5.0x5.0mm_P3.2mm, F.Cu at (182.0, 126.0)
- added D124: WS2812B, LED_SMD:LED_WS2812B_PLCC4_5.0x5.0mm_P3.2mm, F.Cu at (182.0, 133.0)
- added D125: WS2812B, LED_SMD:LED_WS2812B_PLCC4_5.0x5.0mm_P3.2mm, F.Cu at (182.0, 140.0)
- added D126: WS2812B, LED_SMD:LED_WS2812B_PLCC4_5.0x5.0mm_P3.2mm, F.Cu at (182.0, 147.0)
- added D127: WS2812B, LED_SMD:LED_WS2812B_PLCC4_5.0x5.0mm_P3.2mm, F.Cu at (182.0, 154.0)
- added D128: WS2812B, LED_SMD:LED_WS2812B_PLCC4_5.0x5.0mm_P3.2mm, F.Cu at (182.0, 161.0)
- added D129: WS2812B, LED_SMD:LED_WS2812B_PLCC4_5.0x5.0mm_P3.2mm, F.Cu at (189.0, 161.0)
- added D13: WS2812B, LED_SMD:LED_WS2812B_PLCC4_5.0x5.0mm_P3.2mm, F.Cu at (133.0, 77.0)
- added D130: WS2812B, LED_SMD:LED_WS2812B_PLCC4_5.0x5.0mm_P3.2mm, F.Cu at (189.0, 154.0)
- added D131: WS2812B, LED_SMD:LED_WS2812B_PLCC4_5.0x5.0mm_P3.2mm, F.Cu at (189.0, 147.0)
- added D132: WS2812B, LED_SMD:LED_WS2812B_PLCC4_5.0x5.0mm_P3.2mm, F.Cu at (189.0, 140.0)
- added D133: WS2812B, LED_SMD:LED_WS2812B_PLCC4_5.0x5.0mm_P3.2mm, F.Cu at (189.0, 133.0)
- added D134: WS2812B, LED_SMD:LED_WS2812B_PLCC4_5.0x5.0mm_P3.2mm, F.Cu at (189.0, 126.0)
- added D135: WS2812B, LED_SMD:LED_WS2812B_PLCC4_5.0x5.0mm_P3.2mm, F.Cu at (189.0, 119.0)
- added D136: WS2812B, LED_SMD:LED_WS2812B_PLCC4_5.0x5.0mm_P3.2mm, F.Cu at (189.0, 112.0)
- added D137: WS2812B, LED_SMD:LED_WS2812B_PLCC4_5.0x5.0mm_P3.2mm, F.Cu at (189.0, 105.0)
- added D138: WS2812B, LED_SMD:LED_WS2812B_PLCC4_5.0x5.0mm_P3.2mm, F.Cu at (189.0, 98.0)
- added D139: WS2812B, LED_SMD:LED_WS2812B_PLCC4_5.0x5.0mm_P3.2mm, F.Cu at (189.0, 91.0)
- added D14: WS2812B, LED_SMD:LED_WS2812B_PLCC4_5.0x5.0mm_P3.2mm, F.Cu at (133.0, 70.0)
- added D140: WS2812B, LED_SMD:LED_WS2812B_PLCC4_5.0x5.0mm_P3.2mm, F.Cu at (189.0, 84.0)
- added D141: WS2812B, LED_SMD:LED_WS2812B_PLCC4_5.0x5.0mm_P3.2mm, F.Cu at (189.0, 77.0)
- added D142: WS2812B, LED_SMD:LED_WS2812B_PLCC4_5.0x5.0mm_P3.2mm, F.Cu at (189.0, 70.0)
- added D143: WS2812B, LED_SMD:LED_WS2812B_PLCC4_5.0x5.0mm_P3.2mm, F.Cu at (189.0, 63.0)
- added D144: WS2812B, LED_SMD:LED_WS2812B_PLCC4_5.0x5.0mm_P3.2mm, F.Cu at (189.0, 56.0)
- added D145: WS2812B, LED_SMD:LED_WS2812B_PLCC4_5.0x5.0mm_P3.2mm, F.Cu at (196.0, 56.0)
- added D146: WS2812B, LED_SMD:LED_WS2812B_PLCC4_5.0x5.0mm_P3.2mm, F.Cu at (196.0, 63.0)
- added D147: WS2812B, LED_SMD:LED_WS2812B_PLCC4_5.0x5.0mm_P3.2mm, F.Cu at (196.0, 70.0)
- added D148: WS2812B, LED_SMD:LED_WS2812B_PLCC4_5.0x5.0mm_P3.2mm, F.Cu at (196.0, 77.0)
- added D149: WS2812B, LED_SMD:LED_WS2812B_PLCC4_5.0x5.0mm_P3.2mm, F.Cu at (196.0, 84.0)
- added D15: WS2812B, LED_SMD:LED_WS2812B_PLCC4_5.0x5.0mm_P3.2mm, F.Cu at (133.0, 63.0)
- added D150: WS2812B, LED_SMD:LED_WS2812B_PLCC4_5.0x5.0mm_P3.2mm, F.Cu at (196.0, 91.0)
- added D151: WS2812B, LED_SMD:LED_WS2812B_PLCC4_5.0x5.0mm_P3.2mm, F.Cu at (196.0, 98.0)
- added D152: WS2812B, LED_SMD:LED_WS2812B_PLCC4_5.0x5.0mm_P3.2mm, F.Cu at (196.0, 105.0)
- added D153: WS2812B, LED_SMD:LED_WS2812B_PLCC4_5.0x5.0mm_P3.2mm, F.Cu at (196.0, 112.0)
- added D154: WS2812B, LED_SMD:LED_WS2812B_PLCC4_5.0x5.0mm_P3.2mm, F.Cu at (196.0, 119.0)
- added D155: WS2812B, LED_SMD:LED_WS2812B_PLCC4_5.0x5.0mm_P3.2mm, F.Cu at (196.0, 126.0)
- added D156: WS2812B, LED_SMD:LED_WS2812B_PLCC4_5.0x5.0mm_P3.2mm, F.Cu at (196.0, 133.0)
- added D157: WS2812B, LED_SMD:LED_WS2812B_PLCC4_5.0x5.0mm_P3.2mm, F.Cu at (196.0, 140.0)
- added D158: WS2812B, LED_SMD:LED_WS2812B_PLCC4_5.0x5.0mm_P3.2mm, F.Cu at (196.0, 147.0)
- added D159: WS2812B, LED_SMD:LED_WS2812B_PLCC4_5.0x5.0mm_P3.2mm, F.Cu at (196.0, 154.0)
- added D16: WS2812B, LED_SMD:LED_WS2812B_PLCC4_5.0x5.0mm_P3.2mm, F.Cu at (133.0, 56.0)
- added D160: WS2812B, LED_SMD:LED_WS2812B_PLCC4_5.0x5.0mm_P3.2mm, F.Cu at (196.0, 161.0)
- added D161: WS2812B, LED_SMD:LED_WS2812B_PLCC4_5.0x5.0mm_P3.2mm, F.Cu at (203.0, 161.0)
- added D162: WS2812B, LED_SMD:LED_WS2812B_PLCC4_5.0x5.0mm_P3.2mm, F.Cu at (203.0, 154.0)
- added D163: WS2812B, LED_SMD:LED_WS2812B_PLCC4_5.0x5.0mm_P3.2mm, F.Cu at (203.0, 147.0)
- added D164: WS2812B, LED_SMD:LED_WS2812B_PLCC4_5.0x5.0mm_P3.2mm, F.Cu at (203.0, 140.0)
- added D165: WS2812B, LED_SMD:LED_WS2812B_PLCC4_5.0x5.0mm_P3.2mm, F.Cu at (203.0, 133.0)
- added D166: WS2812B, LED_SMD:LED_WS2812B_PLCC4_5.0x5.0mm_P3.2mm, F.Cu at (203.0, 126.0)
- added D167: WS2812B, LED_SMD:LED_WS2812B_PLCC4_5.0x5.0mm_P3.2mm, F.Cu at (203.0, 119.0)
- added D168: WS2812B, LED_SMD:LED_WS2812B_PLCC4_5.0x5.0mm_P3.2mm, F.Cu at (203.0, 112.0)
- added D169: WS2812B, LED_SMD:LED_WS2812B_PLCC4_5.0x5.0mm_P3.2mm, F.Cu at (203.0, 105.0)
- added D17: WS2812B, LED_SMD:LED_WS2812B_PLCC4_5.0x5.0mm_P3.2mm, F.Cu at (140.0, 56.0)
- added D170: WS2812B, LED_SMD:LED_WS2812B_PLCC4_5.0x5.0mm_P3.2mm, F.Cu at (203.0, 98.0)
- added D171: WS2812B, LED_SMD:LED_WS2812B_PLCC4_5.0x5.0mm_P3.2mm, F.Cu at (203.0, 91.0)
- added D172: WS2812B, LED_SMD:LED_WS2812B_PLCC4_5.0x5.0mm_P3.2mm, F.Cu at (203.0, 84.0)
- added D173: WS2812B, LED_SMD:LED_WS2812B_PLCC4_5.0x5.0mm_P3.2mm, F.Cu at (203.0, 77.0)
- added D174: WS2812B, LED_SMD:LED_WS2812B_PLCC4_5.0x5.0mm_P3.2mm, F.Cu at (203.0, 70.0)
- added D175: WS2812B, LED_SMD:LED_WS2812B_PLCC4_5.0x5.0mm_P3.2mm, F.Cu at (203.0, 63.0)
- added D176: WS2812B, LED_SMD:LED_WS2812B_PLCC4_5.0x5.0mm_P3.2mm, F.Cu at (203.0, 56.0)
- added D177: WS2812B, LED_SMD:LED_WS2812B_PLCC4_5.0x5.0mm_P3.2mm, F.Cu at (210.0, 56.0)
- added D178: WS2812B, LED_SMD:LED_WS2812B_PLCC4_5.0x5.0mm_P3.2mm, F.Cu at (210.0, 63.0)
- added D179: WS2812B, LED_SMD:LED_WS2812B_PLCC4_5.0x5.0mm_P3.2mm, F.Cu at (210.0, 70.0)
- added D18: WS2812B, LED_SMD:LED_WS2812B_PLCC4_5.0x5.0mm_P3.2mm, F.Cu at (140.0, 63.0)
- added D180: WS2812B, LED_SMD:LED_WS2812B_PLCC4_5.0x5.0mm_P3.2mm, F.Cu at (210.0, 77.0)
- added D181: WS2812B, LED_SMD:LED_WS2812B_PLCC4_5.0x5.0mm_P3.2mm, F.Cu at (210.0, 84.0)
- added D182: WS2812B, LED_SMD:LED_WS2812B_PLCC4_5.0x5.0mm_P3.2mm, F.Cu at (210.0, 91.0)
- added D183: WS2812B, LED_SMD:LED_WS2812B_PLCC4_5.0x5.0mm_P3.2mm, F.Cu at (210.0, 98.0)
- added D184: WS2812B, LED_SMD:LED_WS2812B_PLCC4_5.0x5.0mm_P3.2mm, F.Cu at (210.0, 105.0)
- added D185: WS2812B, LED_SMD:LED_WS2812B_PLCC4_5.0x5.0mm_P3.2mm, F.Cu at (210.0, 112.0)
- added D186: WS2812B, LED_SMD:LED_WS2812B_PLCC4_5.0x5.0mm_P3.2mm, F.Cu at (210.0, 119.0)
- added D187: WS2812B, LED_SMD:LED_WS2812B_PLCC4_5.0x5.0mm_P3.2mm, F.Cu at (210.0, 126.0)
- added D188: WS2812B, LED_SMD:LED_WS2812B_PLCC4_5.0x5.0mm_P3.2mm, F.Cu at (210.0, 133.0)
- added D189: WS2812B, LED_SMD:LED_WS2812B_PLCC4_5.0x5.0mm_P3.2mm, F.Cu at (210.0, 140.0)
- added D19: WS2812B, LED_SMD:LED_WS2812B_PLCC4_5.0x5.0mm_P3.2mm, F.Cu at (140.0, 70.0)
- added D190: WS2812B, LED_SMD:LED_WS2812B_PLCC4_5.0x5.0mm_P3.2mm, F.Cu at (210.0, 147.0)
- added D191: WS2812B, LED_SMD:LED_WS2812B_PLCC4_5.0x5.0mm_P3.2mm, F.Cu at (210.0, 154.0)
- added D192: WS2812B, LED_SMD:LED_WS2812B_PLCC4_5.0x5.0mm_P3.2mm, F.Cu at (210.0, 161.0)
- added D193: WS2812B, LED_SMD:LED_WS2812B_PLCC4_5.0x5.0mm_P3.2mm, F.Cu at (217.0, 161.0)
- added D194: WS2812B, LED_SMD:LED_WS2812B_PLCC4_5.0x5.0mm_P3.2mm, F.Cu at (217.0, 154.0)
- added D195: WS2812B, LED_SMD:LED_WS2812B_PLCC4_5.0x5.0mm_P3.2mm, F.Cu at (217.0, 147.0)
- added D196: WS2812B, LED_SMD:LED_WS2812B_PLCC4_5.0x5.0mm_P3.2mm, F.Cu at (217.0, 140.0)
- added D197: WS2812B, LED_SMD:LED_WS2812B_PLCC4_5.0x5.0mm_P3.2mm, F.Cu at (217.0, 133.0)
- added D198: WS2812B, LED_SMD:LED_WS2812B_PLCC4_5.0x5.0mm_P3.2mm, F.Cu at (217.0, 126.0)
- added D199: WS2812B, LED_SMD:LED_WS2812B_PLCC4_5.0x5.0mm_P3.2mm, F.Cu at (217.0, 119.0)
- added D2: WS2812B, LED_SMD:LED_WS2812B_PLCC4_5.0x5.0mm_P3.2mm, F.Cu at (133.0, 154.0)
- added D20: WS2812B, LED_SMD:LED_WS2812B_PLCC4_5.0x5.0mm_P3.2mm, F.Cu at (140.0, 77.0)
- added D200: WS2812B, LED_SMD:LED_WS2812B_PLCC4_5.0x5.0mm_P3.2mm, F.Cu at (217.0, 112.0)
- added D201: WS2812B, LED_SMD:LED_WS2812B_PLCC4_5.0x5.0mm_P3.2mm, F.Cu at (217.0, 105.0)
- added D202: WS2812B, LED_SMD:LED_WS2812B_PLCC4_5.0x5.0mm_P3.2mm, F.Cu at (217.0, 98.0)
- added D203: WS2812B, LED_SMD:LED_WS2812B_PLCC4_5.0x5.0mm_P3.2mm, F.Cu at (217.0, 91.0)
- added D204: WS2812B, LED_SMD:LED_WS2812B_PLCC4_5.0x5.0mm_P3.2mm, F.Cu at (217.0, 84.0)
- added D205: WS2812B, LED_SMD:LED_WS2812B_PLCC4_5.0x5.0mm_P3.2mm, F.Cu at (217.0, 77.0)
- added D206: WS2812B, LED_SMD:LED_WS2812B_PLCC4_5.0x5.0mm_P3.2mm, F.Cu at (217.0, 70.0)
- added D207: WS2812B, LED_SMD:LED_WS2812B_PLCC4_5.0x5.0mm_P3.2mm, F.Cu at (217.0, 63.0)
- added D208: WS2812B, LED_SMD:LED_WS2812B_PLCC4_5.0x5.0mm_P3.2mm, F.Cu at (217.0, 56.0)
- added D209: WS2812B, LED_SMD:LED_WS2812B_PLCC4_5.0x5.0mm_P3.2mm, F.Cu at (224.0, 56.0)
- added D21: WS2812B, LED_SMD:LED_WS2812B_PLCC4_5.0x5.0mm_P3.2mm, F.Cu at (140.0, 84.0)
- added D210: WS2812B, LED_SMD:LED_WS2812B_PLCC4_5.0x5.0mm_P3.2mm, F.Cu at (224.0, 63.0)
- added D211: WS2812B, LED_SMD:LED_WS2812B_PLCC4_5.0x5.0mm_P3.2mm, F.Cu at (224.0, 70.0)
- added D212: WS2812B, LED_SMD:LED_WS2812B_PLCC4_5.0x5.0mm_P3.2mm, F.Cu at (224.0, 77.0)
- added D213: WS2812B, LED_SMD:LED_WS2812B_PLCC4_5.0x5.0mm_P3.2mm, F.Cu at (224.0, 84.0)
- added D214: WS2812B, LED_SMD:LED_WS2812B_PLCC4_5.0x5.0mm_P3.2mm, F.Cu at (224.0, 91.0)
- added D215: WS2812B, LED_SMD:LED_WS2812B_PLCC4_5.0x5.0mm_P3.2mm, F.Cu at (224.0, 98.0)
- added D216: WS2812B, LED_SMD:LED_WS2812B_PLCC4_5.0x5.0mm_P3.2mm, F.Cu at (224.0, 105.0)
- added D217: WS2812B, LED_SMD:LED_WS2812B_PLCC4_5.0x5.0mm_P3.2mm, F.Cu at (224.0, 112.0)
- added D218: WS2812B, LED_SMD:LED_WS2812B_PLCC4_5.0x5.0mm_P3.2mm, F.Cu at (224.0, 119.0)
- added D219: WS2812B, LED_SMD:LED_WS2812B_PLCC4_5.0x5.0mm_P3.2mm, F.Cu at (224.0, 126.0)
- added D22: WS2812B, LED_SMD:LED_WS2812B_PLCC4_5.0x5.0mm_P3.2mm, F.Cu at (140.0, 91.0)
- added D220: WS2812B, LED_SMD:LED_WS2812B_PLCC4_5.0x5.0mm_P3.2mm, F.Cu at (224.0, 133.0)
- added D221: WS2812B, LED_SMD:LED_WS2812B_PLCC4_5.0x5.0mm_P3.2mm, F.Cu at (224.0, 140.0)
- added D222: WS2812B, LED_SMD:LED_WS2812B_PLCC4_5.0x5.0mm_P3.2mm, F.Cu at (224.0, 147.0)
- added D223: WS2812B, LED_SMD:LED_WS2812B_PLCC4_5.0x5.0mm_P3.2mm, F.Cu at (224.0, 154.0)
- added D224: WS2812B, LED_SMD:LED_WS2812B_PLCC4_5.0x5.0mm_P3.2mm, F.Cu at (224.0, 161.0)
- added D225: WS2812B, LED_SMD:LED_WS2812B_PLCC4_5.0x5.0mm_P3.2mm, F.Cu at (231.0, 161.0)
- added D226: WS2812B, LED_SMD:LED_WS2812B_PLCC4_5.0x5.0mm_P3.2mm, F.Cu at (231.0, 154.0)
- added D227: WS2812B, LED_SMD:LED_WS2812B_PLCC4_5.0x5.0mm_P3.2mm, F.Cu at (231.0, 147.0)
- added D228: WS2812B, LED_SMD:LED_WS2812B_PLCC4_5.0x5.0mm_P3.2mm, F.Cu at (231.0, 140.0)
- added D229: WS2812B, LED_SMD:LED_WS2812B_PLCC4_5.0x5.0mm_P3.2mm, F.Cu at (231.0, 133.0)
- added D23: WS2812B, LED_SMD:LED_WS2812B_PLCC4_5.0x5.0mm_P3.2mm, F.Cu at (140.0, 98.0)
- added D230: WS2812B, LED_SMD:LED_WS2812B_PLCC4_5.0x5.0mm_P3.2mm, F.Cu at (231.0, 126.0)
- added D231: WS2812B, LED_SMD:LED_WS2812B_PLCC4_5.0x5.0mm_P3.2mm, F.Cu at (231.0, 119.0)
- added D232: WS2812B, LED_SMD:LED_WS2812B_PLCC4_5.0x5.0mm_P3.2mm, F.Cu at (231.0, 112.0)
- added D233: WS2812B, LED_SMD:LED_WS2812B_PLCC4_5.0x5.0mm_P3.2mm, F.Cu at (231.0, 105.0)
- added D234: WS2812B, LED_SMD:LED_WS2812B_PLCC4_5.0x5.0mm_P3.2mm, F.Cu at (231.0, 98.0)
- added D235: WS2812B, LED_SMD:LED_WS2812B_PLCC4_5.0x5.0mm_P3.2mm, F.Cu at (231.0, 91.0)
- added D236: WS2812B, LED_SMD:LED_WS2812B_PLCC4_5.0x5.0mm_P3.2mm, F.Cu at (231.0, 84.0)
- added D237: WS2812B, LED_SMD:LED_WS2812B_PLCC4_5.0x5.0mm_P3.2mm, F.Cu at (231.0, 77.0)
- added D238: WS2812B, LED_SMD:LED_WS2812B_PLCC4_5.0x5.0mm_P3.2mm, F.Cu at (231.0, 70.0)
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- renumbered C3 to C2, C4 to C3, C10 to C4, C9 to C5, J5 to J2, Q4 to Q2, R28 to R1, R25 to R2, R27 to R4, R18 to R5, R16 to R6, R17 to R7, TP2 to TP1, TP1 to TP2, U3 to U2, U4 to U3, U11 to U4
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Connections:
- net Net-(J1-Pad1) renamed /Vbus
- net Net-(J1-Pad2) renamed /Dm
- net Net-(J1-Pad3) renamed /Dp
- J3 pad 1: +5V -> +3V3
- J3 pad 2: Net-(J3-Pad2) -> +5V
- J3 pad 3: GND -> /IO36
- J4 pad 1: +3V3 -> +5V
- J4 pad 2: /IO36 -> GND
- J4 pad 3: /IO39 -> GND
- U1 pad 5: Net-(J3-Pad2) -> Net-(R3-Pad2)
- U3 pad 12: /IO27 -> /DOUT
- U3 pad 37: /DOUT -> Net-(U3-Pad37)
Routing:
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- added copper zone on F.Cu, net +5V
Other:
- board size 61 x 42.5 mm -> 114 x 153 mm
- rule pad_to_mask_clearance: 0.2 -> 0
- board text added: "5V"
- board text added: "DO"
- board text added: "ESP32LedControl Rev1"
- board text added: "LED_SIG"
- board text removed: "Dout"
- board text removed: "Gnd"
- board text removed: "IO27"
- board text removed: "RESET"
- board text removed: "Vcc"
